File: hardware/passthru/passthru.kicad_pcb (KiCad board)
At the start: 2 copper layers, 63.5 x 59.7 mm, 83 parts, among them J1 ARM_SWD, J2 RJ45_LED_Shielded, J3 Screw_Terminal_01x02, Q1 Q_PMOS_DGS, Q2 Q_PMOS_DGS, Q3 Q_NPN_BEC, U1 EFM32GG11B8xx, U2 KSZ8081RND, U3 LM5085, U4 TPS2375-1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

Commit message: passthru: various cleanup
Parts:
- moved R18 1.27 mm to (122.6, 83.8)
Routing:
- net GND: track 92.0 -> 81.2 mm
- net +3V3: track 124.3 -> 120.6 mm
- net VDD: track 102.2 -> 99.7 mm
- net /LOAD_SEN: track 66.0 -> 65.0 mm
- added copper zone on F.Cu, net +3V3
- added copper zone on F.Cu, net GND
- added copper zone on F.Cu, net Net-(C25-Pad1)
- added copper zone on F.Cu, net VDD

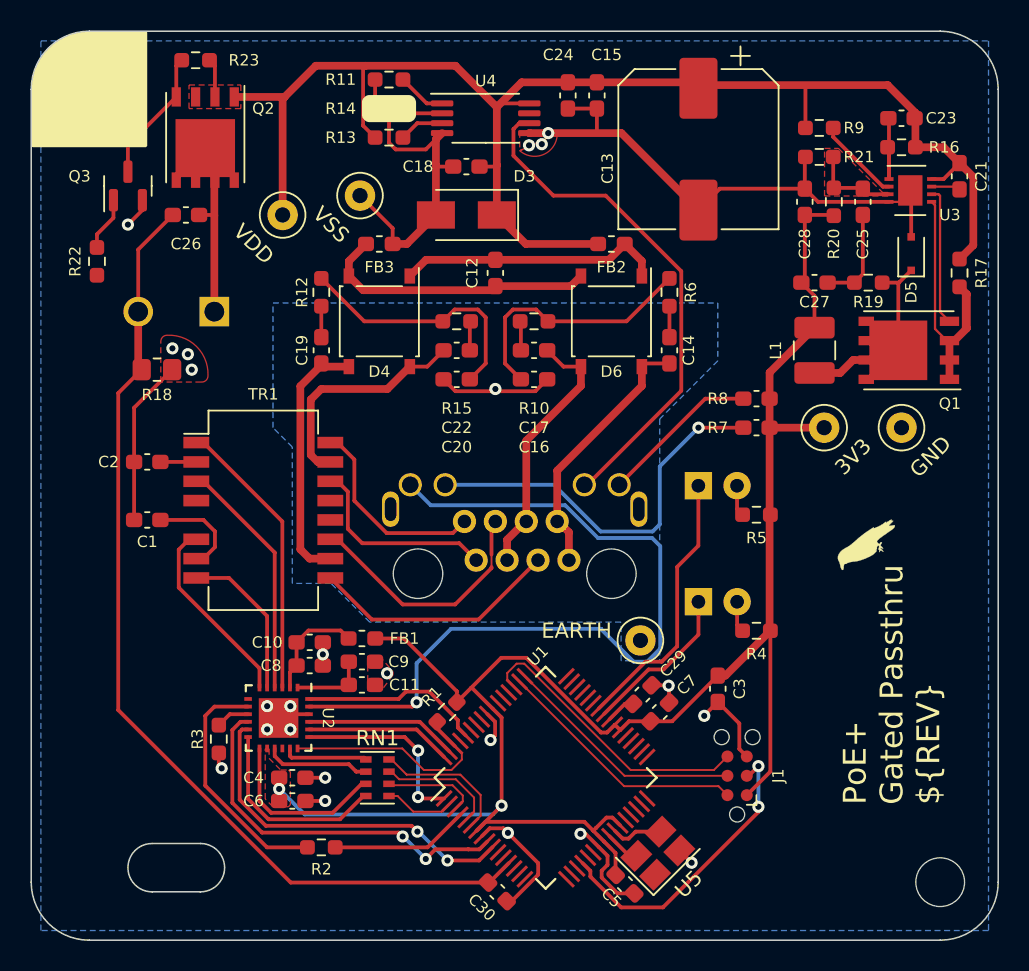
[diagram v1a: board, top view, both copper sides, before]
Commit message: passthru: use local footprint for PFETs
This one has 3D models.
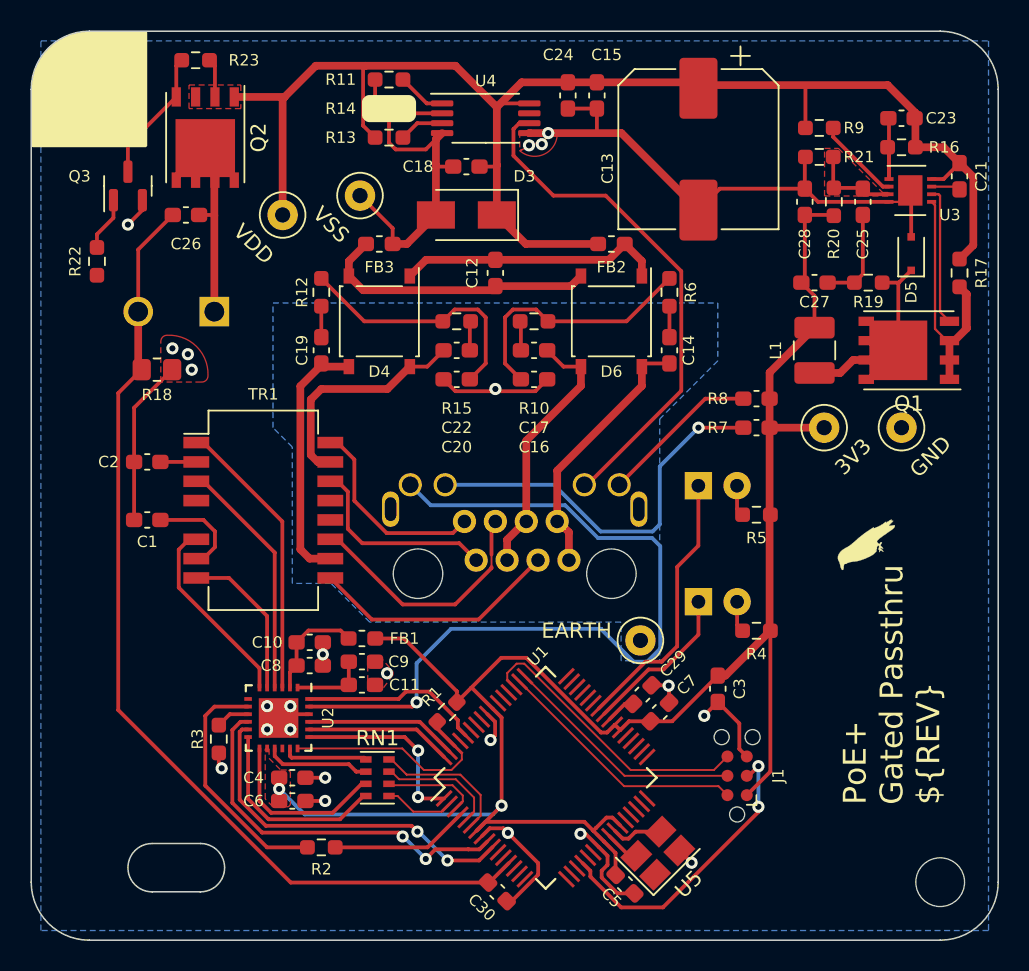
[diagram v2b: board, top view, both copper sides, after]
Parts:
- Q1, Q2: footprint Package_SO:PowerPAK_SO-8_Single -> common:PowerPAK_SO-8_Single
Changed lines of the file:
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@@
     )
   )
-  (footprint "Package_SO:PowerPAK_SO-8_Single" (layer "F.Cu")
+  (footprint "common:PowerPAK_SO-8_Single" (layer "F.Cu")
     (at 171.9295 82.55 180)
     (descr "PowerPAK SO-8 Single (https://www.vishay.com/docs/71655/powerpak.pdf, https://www.vishay.com/docs/72599/72599.pdf)")
@@
     (property "Sheetname" "")
     (attr smd)
-    (fp_text reference "Q1" (at -2.6955 -3.5) (layer "F.SilkS")
-      (effects (font (size 0.75 0.75) (thickness 0.15)))
-    )
-    (fp_text value "Q_PMOS_DGS" (at 0 3.5) (layer "F.Fab")
-      (effects (font (size 1 1) (thickness 0.15)))
-    )
-    (fp_text user "${REFERENCE}" (at 0 0) (layer "F.Fab")
+    (fp_text reference "Q1" (at 0 -3.5 180) (layer "F.SilkS")
+      (effects (font (size 1 1) (thickness 0.15)))
+    )
+    (fp_text value "Q_PMOS_DGS" (at 0 3.5 180) (layer "F.Fab")
+      (effects (font (size 1 1) (thickness 0.15)))
+    )
+    (fp_text user "${REFERENCE}" (at 0 0 180) (layer "F.Fab")
       (effects (font (size 1 1) (thickness 0.15)))
     )
     (fp_line (start -2.945 2.57) (end 2.945 2.57) (layer "F.SilkS") (width 0.12))
     (fp_line (start -3.4 -2.57) (end 2.945 -2.57) (layer "F.SilkS") (width 0.12))
+    (fp_line (start -3.55 -2.75) (end -3.55 2.75) (layer "F.CrtYd") (width 0.05))
+    (fp_line (start 3.55 -2.75) (end 3.55 2.75) (layer "F.CrtYd") (width 0.05))
     (fp_line (start -3.55 2.75) (end 3.55 2.75) (layer "F.CrtYd") (width 0.05))
     (fp_line (start -3.55 -2.75) (end 3.55 -2.75) (layer "F.CrtYd") (width 0.05))
-    (fp_line (start -3.55 -2.75) (end -3.55 2.75) (layer "F.CrtYd") (width 0.05))
-    (fp_line (start 3.55 -2.75) (end 3.55 2.75) (layer "F.CrtYd") (width 0.05))
-    (fp_line (start -1.945 -2.45) (end -2.945 -1.45) (layer "F.Fab") (width 0.1))
-    (fp_line (start -1.945 -2.45) (end 2.945 -2.45) (layer "F.Fab") (width 0.1))
     (fp_line (start 2.945 2.45) (end -2.945 2.45) (layer "F.Fab") (width 0.1))
     (fp_line (start -2.945 2.45) (end -2.945 -1.45) (layer "F.Fab") (width 0.1))
+    (fp_line (start -1.945 -2.45) (end -2.945 -1.45) (layer "F.Fab") (width 0.1))
     (fp_line (start 2.945 -2.45) (end 2.945 2.45) (layer "F.Fab") (width 0.1))
+    (fp_line (start -1.945 -2.45) (end 2.945 -2.45) (layer "F.Fab") (width 0.1))
     (pad "1" smd rect (at -2.67 -1.905 180) (size 1.27 0.61) (layers "F.Cu" "F.Paste" "F.Mask")
       (net 106 "Net-(Q1-Pad1)") (pinfunction "S") (pintype "passive"))
@@
     (pad "5" smd rect (at 2.795 1.905 180) (size 1.02 0.61) (layers "F.Cu" "F.Paste" "F.Mask")
       (net 91 "Net-(D5-Pad1)") (pinfunction "D") (pintype "passive"))
-    (pad "5" smd rect (at 0.69 0 180) (size 3.81 3.91) (layers "F.Cu" "F.Paste" "F.Mask")
+    (pad "5" smd rect (at 2.795 -1.905 180) (size 1.02 0.61) (layers "F.Cu" "F.Paste" "F.Mask")
       (net 91 "Net-(D5-Pad1)") (pinfunction "D") (pintype "passive"))
     (pad "5" smd rect (at 2.795 0.635 180) (size 1.02 0.61) (layers "F.Cu" "F.Paste" "F.Mask")
@@
     (pad "5" smd rect (at 2.795 -0.635 180) (size 1.02 0.61) (layers "F.Cu" "F.Paste" "F.Mask")
       (net 91 "Net-(D5-Pad1)") (pinfunction "D") (pintype "passive"))
-    (pad "5" smd rect (at 2.795 -1.905 180) (size 1.02 0.61) (layers "F.Cu" "F.Paste" "F.Mask")
+    (pad "5" smd rect (at 0.69 0 180) (size 3.81 3.91) (layers "F.Cu" "F.Paste" "F.Mask")
       (net 91 "Net-(D5-Pad1)") (pinfunction "D") (pintype "passive"))
-    (model "${KICAD6_3DMODEL_DIR}/Package_SO.3dshapes/PowerPAK_SO-8_Single.wrl"
+    (model "${KIPRJMOD}/../common/common.3dshapes/PowerPAK SO-8.step"
       (offset (xyz 0 0 0))
       (scale (xyz 1 1 1))
@@
     )
   )
-  (footprint "Package_SO:PowerPAK_SO-8_Single" (layer "F.Cu")
+  (footprint "common:PowerPAK_SO-8_Single" (layer "F.Cu")
     (at 125.73 68.58 -90)
     (descr "PowerPAK SO-8 Single (https://www.vishay.com/docs/71655/powerpak.pdf, https://www.vishay.com/docs/72599/72599.pdf)")
@@
     (property "Sheetname" "")
     (attr smd)
-    (fp_text reference "Q2" (at -1.905 -3.81 180) (layer "F.SilkS")
-      (effects (font (size 0.75 0.75) (thickness 0.15)))
-    )
-    (fp_text value "Q_PMOS_DGS" (at 0 3.5 90) (layer "F.Fab")
-      (effects (font (size 1 1) (thickness 0.15)))
-    )
-    (fp_text user "${REFERENCE}" (at 0 0 90) (layer "F.Fab")
+    (fp_text reference "Q2" (at 0 -3.5 -90) (layer "F.SilkS")
+      (effects (font (size 1 1) (thickness 0.15)))
+    )
+    (fp_text value "Q_PMOS_DGS" (at 0 3.5 -90) (layer "F.Fab")
+      (effects (font (size 1 1) (thickness 0.15)))
+    )
+    (fp_text user "${REFERENCE}" (at 0 0 -90) (layer "F.Fab")
       (effects (font (size 1 1) (thickness 0.15)))
     )
@@
     (fp_line (start -3.55 -2.75) (end -3.55 2.75) (layer "F.CrtYd") (width 0.05))
     (fp_line (start -3.55 -2.75) (end 3.55 -2.75) (layer "F.CrtYd") (width 0.05))
+    (fp_line (start 2.945 2.45) (end -2.945 2.45) (layer "F.Fab") (width 0.1))
+    (fp_line (start -1.945 -2.45) (end -2.945 -1.45) (layer "F.Fab") (width 0.1))
+    (fp_line (start -1.945 -2.45) (end 2.945 -2.45) (layer "F.Fab") (width 0.1))
     (fp_line (start 2.945 -2.45) (end 2.945 2.45) (layer "F.Fab") (width 0.1))
-    (fp_line (start -1.945 -2.45) (end 2.945 -2.45) (layer "F.Fab") (width 0.1))
-    (fp_line (start 2.945 2.45) (end -2.945 2.45) (layer "F.Fab") (width 0.1))
     (fp_line (start -2.945 2.45) (end -2.945 -1.45) (layer "F.Fab") (width 0.1))
-    (fp_line (start -1.945 -2.45) (end -2.945 -1.45) (layer "F.Fab") (width 0.1))
     (pad "1" smd rect (at -2.67 -1.905 270) (size 1.27 0.61) (layers "F.Cu" "F.Paste" "F.Mask")
       (net 5 "VDD") (pinfunction "S") (pintype "passive"))
@@
     (pad "5" smd rect (at 2.795 0.635 270) (size 1.02 0.61) (layers "F.Cu" "F.Paste" "F.Mask")
       (net 99 "Net-(C26-Pad1)") (pinfunction "D") (pintype "passive"))
-    (model "${KICAD6_3DMODEL_DIR}/Package_SO.3dshapes/PowerPAK_SO-8_Single.wrl"
+    (model "${KIPRJMOD}/../common/common.3dshapes/PowerPAK SO-8.step"
       (offset (xyz 0 0 0))
       (scale (xyz 1 1 1))
@@
     (property "Sheetname" "")
     (attr smd)
-    (fp_text reference "U2" (at 0 -3.25 -90 unlocked) (layer "F.SilkS")
-      (effects (font (size 0.75 0.75) (thickness 0.15)))
-    )
+    (fp_text reference "U2" (at 0 -3.25 -90) (layer "F.SilkS")
+      (effects (font (size 0.75 0.75) (thickness 0.15)))
+    )
